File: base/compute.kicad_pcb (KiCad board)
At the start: 4 copper layers, 87.7 x 62.8 mm, 124 parts, among them IC1 TMC2209-LA-T, IC2 TMC2209-LA-T, IC3 TMC2209-LA-T, IC4 DMP6023LSS-13, J1 USB_C_Receptacle_USB2.0_16P, J13 fan, J2 Conn_01x20, J3 2-84952-0, J4 DC_Jack_5.5x2.5, J9 spindle, Q1 Q_NMOS_GDS_spindle, Q2 Q_NMOS_GSD_fan, SW1 SW_Push_Open, SW2 SW_Push_Open, U1 MCP1700T-1202ETT, U2 ESP32-S3-WROOM-2, U3 LD1117S33TR_SOT223, U4 MCP1700-1502, U5 ICE40UP5K-SG48ITR-FPGA_Lattice, U6 MCP1700T-2802E, U7 USBLC6-2SC6, U8 AP63203WU-7

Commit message: send to fab
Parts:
- added C57: 0.1uF, Capacitor_SMD:C_0805_2012Metric_Pad1.18x1.45mm_HandSolder, F.Cu at (208.8, 157.9)
- FL1: footprint Inductor_SMD:L_CommonModeChoke_Coilcraft_0603USB -> footprints:L_CommonModeChoke_Coilcraft_0603USB
- H1, H2, H3, H4: footprint MountingHole:MountingHole_2.2mm_M2_Pad_Via -> MountingHole:MountingHole_2.5mm_Pad_Via
- J2: value Conn_01x20 -> FPC-24P-0.5mm
- R2, R26, R28, R29, R3, R30, R31, R4, R7: value 10K -> 5.1K
- R27: value 140K -> 71.5K
- R8, R9: value 1.5K -> 5.1K
- U3: value LD1117S33TR_SOT223 -> LM1117MPX-5.0/NOPB; footprint Package_TO_SOT_SMD:SOT-23 -> Package_TO_SOT_SMD:SOT-223-3_TabPin2
- moved C1 10.6 mm to (197.2, 157.1), turned to 180 degrees
- moved C10 9.91 mm to (193.7, 160.8), turned to 180 degrees
- moved C17 2.54 mm to (194.5, 149.1)
- moved C19 2.19 mm to (194.8, 154.7)
- moved U4 2.19 mm to (194.7, 151.9)
- moved U3 1.29 mm to (200.6, 151.7), turned to 90 degrees
- moved C55 1.22 mm to (193.1, 156.9)
- moved C11 0.53 mm to (206.2, 154.9), turned to 0 degrees
- moved J1 0.36 mm to (181.6, 190.4)
- moved C21 0.35 mm to (201.1, 157.1)
- moved SW2 0.30 mm to (179.3, 134.4)
- moved C12 0.21 mm to (197.4, 145.9), turned to 0 degrees
- turned U1 to 180 degrees
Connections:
- IC1 pad 17: +3.3V -> unconnected-(IC1-VREF-Pad17)
- IC2 pad 17: +3.3V -> unconnected-(IC2-VREF-Pad17)
- IC3 pad 17: +3.3V -> unconnected-(IC3-VREF-Pad17)
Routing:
- net GND: track 227.7 -> 251.2 mm
- net +12V: track 118.5 -> 130.9 mm
- net +5V: track 28.6 -> 37.3 mm
- net +3.3V: track 274.9 -> 270.5 mm
- net +5VUSBC: track 36.5 -> 33.9 mm
- net +2V8: track 30.4 -> 32.4 mm
- net +1V5: track 22.5 -> 24.3 mm
- net +1V2: track 37.9 -> 36.5 mm
- net CAM_RST: track 34.7 -> 33.8 mm
- net Net-(F1-Pad1): track 15.8 -> 16.4 mm
- net Net-(J1-D+-PadA6): track 31.8 -> 32.4 mm
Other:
- board size 87.7 x 62.8 mm -> 88.4 x 63.6 mm

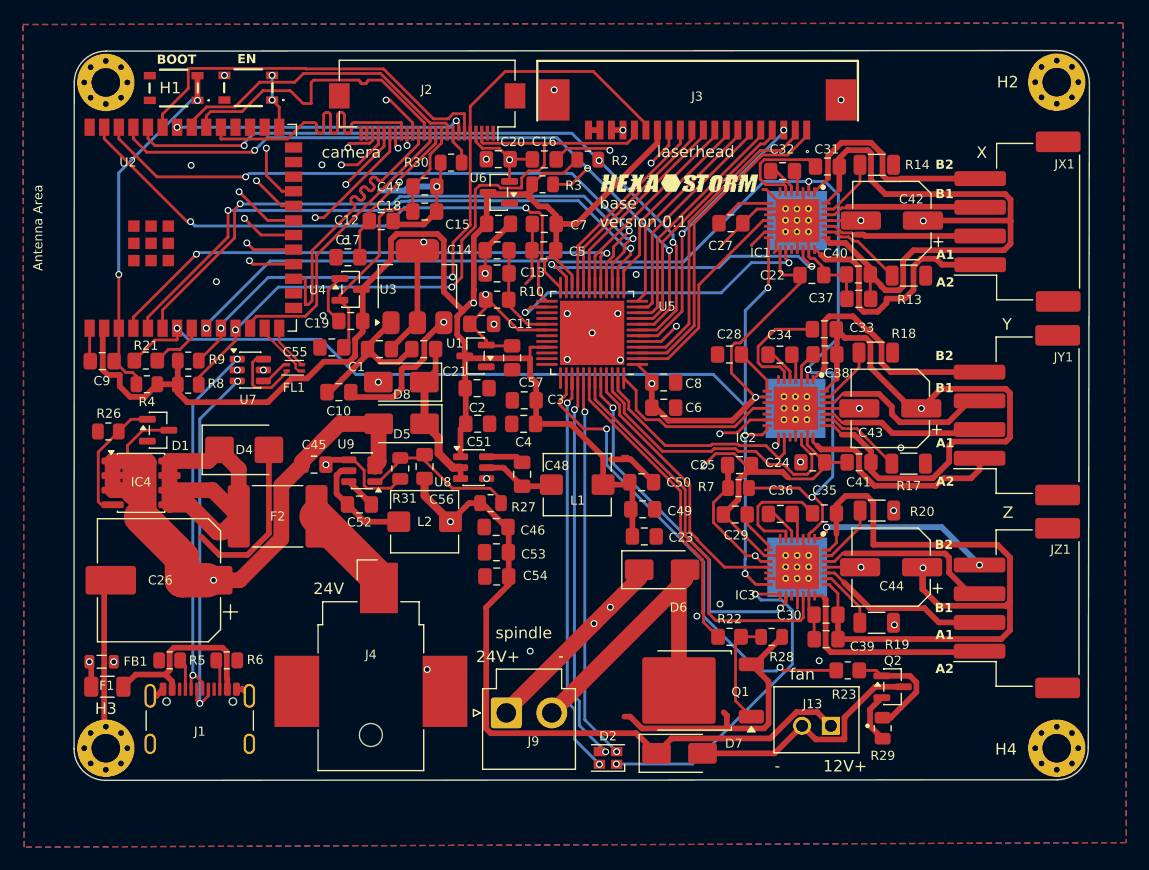
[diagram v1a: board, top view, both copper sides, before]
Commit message: fixed: uartx res to 5.1K, switch connection cross, camera connextor top side
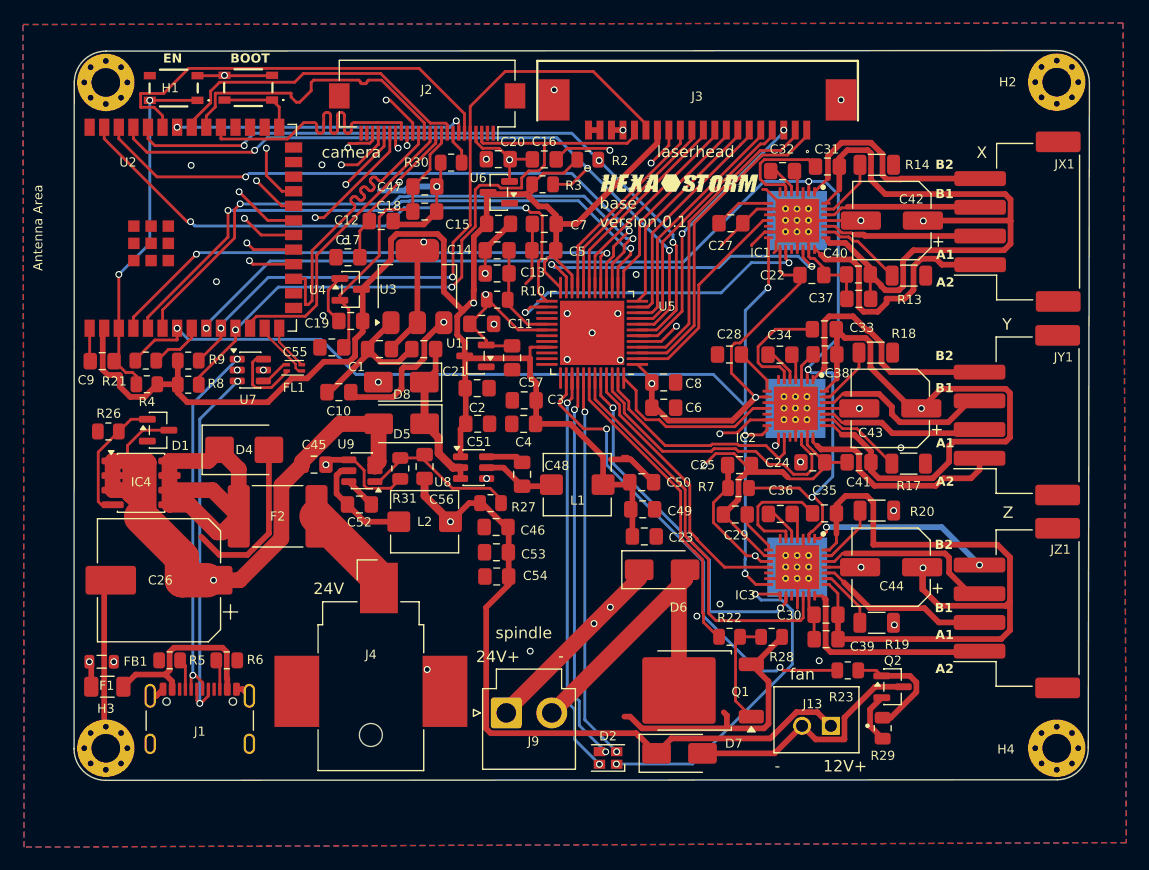
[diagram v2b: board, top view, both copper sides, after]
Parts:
- R10, R22, R23: footprint Resistor_SMD:R_0805_2012Metric_Pad1.20x1.40mm_HandSolder -> Resistor_SMD:R_0805_2012Metric
- R21: value 1K -> 5.1K; footprint Resistor_SMD:R_0805_2012Metric_Pad1.20x1.40mm_HandSolder -> Resistor_SMD:R_0805_2012Metric
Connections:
- SW1 pad 2: GND -> Net-(U2-GPIO0/BOOT)
- SW1 pad 3: Net-(U2-GPIO0/BOOT) -> GND
- SW2 pad 2: GND -> Net-(U2-EN)
- SW2 pad 3: Net-(U2-EN) -> GND
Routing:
- net GND: track 251.2 -> 257.8 mm
- net CAM_RST: track 33.8 -> 36.9 mm
- net Net-(U2-GPIO0/BOOT): track 4.78 -> 6.78 mm, vias 2 -> 0
- net DVP_HREF: track 27.1 -> 27.7 mm
